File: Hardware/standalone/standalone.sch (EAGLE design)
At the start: 87 parts, among them Q2 32.768khz, U1 DMS3016SSS-13, U2 DMS3016SSS-13, U3 DMS3016SSS-13, U4 LM2575S-15, U5 NMOS_2N7002, U6 NMOS_2N7002, X1 KUSBVX, X2 KUSBVX

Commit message: Added item to hardware todo list
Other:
- note added: "TODO: - Change Caps to surface mount - Battery Bi-Directional Current Sense - Change Current Sense R - Swap 5V Diode to SMT - Power LED - Check if LCD R/W Pin is needed?"
- note removed: "TODO: - Change Caps to surface mount - Battery Bi-Directional Current Sense - Change Current Sense R - Swap 5V Diode to SMT - Power LED"
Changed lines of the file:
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@@
   - Change Current Sense R
   - Swap 5V Diode to SMT
-  - Power LED</text>
+  - Power LED
+  - Check if LCD R/W Pin is needed?</text>
 </plain>
 <instances>

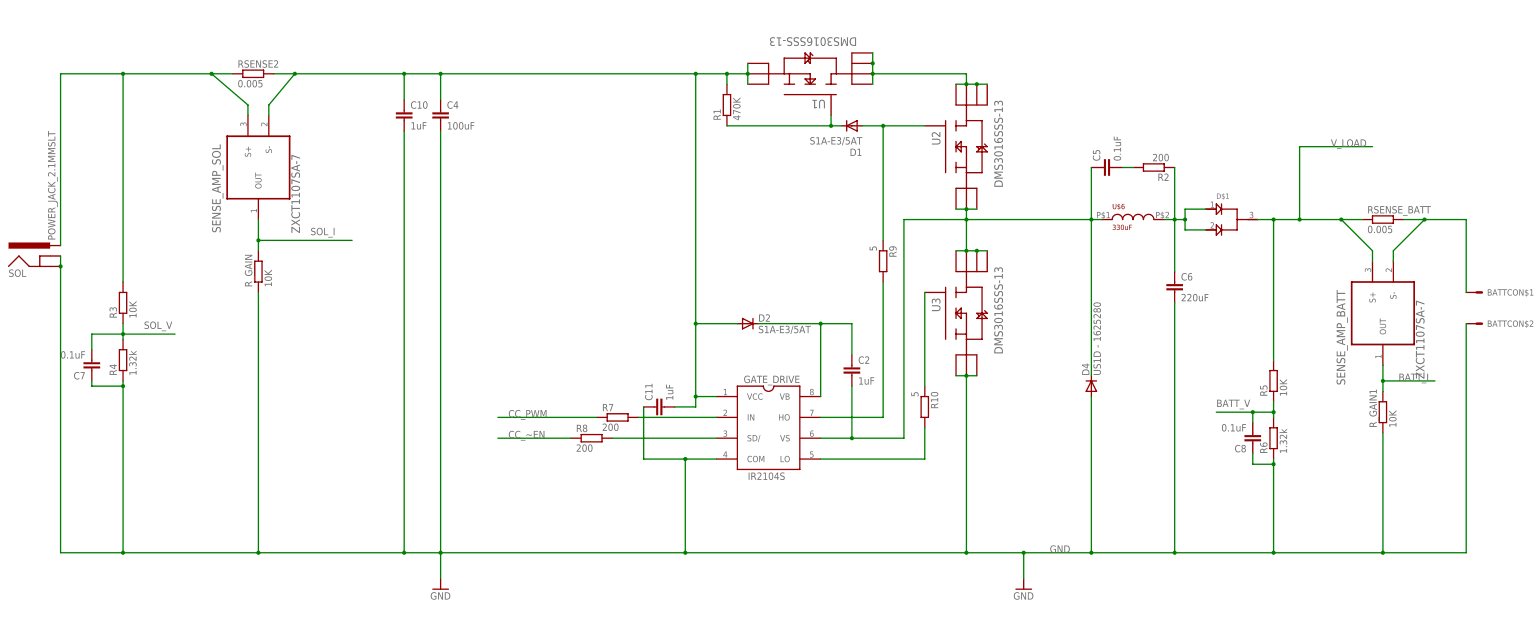
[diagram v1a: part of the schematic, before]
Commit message: Some Hardware Fixes
Fixed the Battery Connector.
Added more items to ToDo list
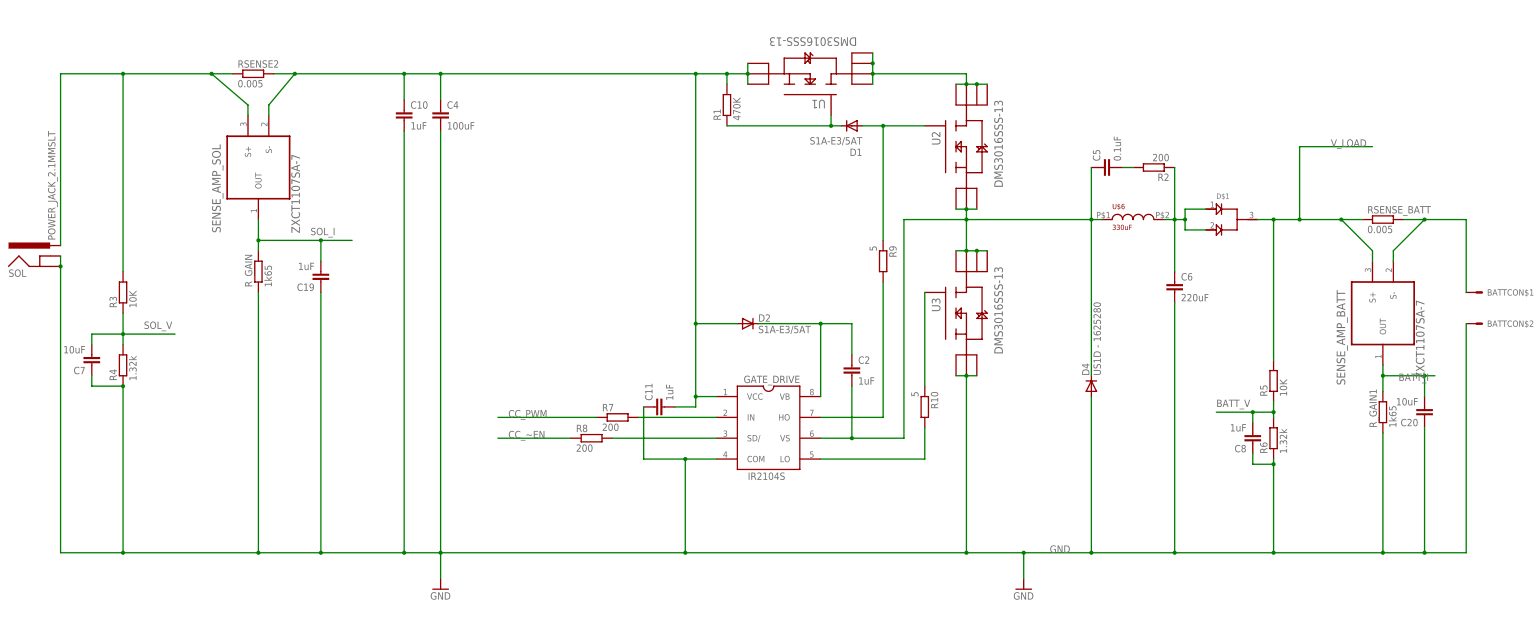
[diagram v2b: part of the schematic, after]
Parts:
- added C19: 1uF, resistor:C-EUC0805K
- added C20: 10uF, resistor:C-EUC0805K
- C7: value 0.1uF -> 10uF
- C8: value 0.1uF -> 1uF
- R_GAIN, R_GAIN1: value 10K -> 1k65
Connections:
- net BATT_I: now also C20.2
- net GND: now also C19.1, C20.1
- net SOL_I: now also C19.2
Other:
- note added: "TODO: - Change Caps to surface mount - Battery Bi-Directional Current Sense - Change Current Sense R - Swap 5V Diode to SMT - Power LED - Check if LCD R/W Pin is needed? - Add filtering (LC) to AVCC - Change Battery Diode to: 1336556 - Change Inductors and Cap for Buck - Remove U1 (Not needed) - Change Power Switch"
- note removed: "TODO: - Change Caps to surface mount - Battery Bi-Directional Current Sense - Change Current Sense R - Swap 5V Diode to SMT - Power LED - Check if LCD R/W Pin is needed?"
- moved on the sheet: C7, R3, R4
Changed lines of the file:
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@@
 <part name="R3" library="rcl" deviceset="R-EU_" device="M0805" value="10K"/>
 <part name="R4" library="rcl" deviceset="R-EU_" device="M0805" value="1.32k"/>
-<part name="C7" library="resistor" deviceset="C-EU" device="C0805K" value="0.1uF"/>
+<part name="C7" library="resistor" deviceset="C-EU" device="C0805K" value="10uF"/>
 <part name="R5" library="rcl" deviceset="R-EU_" device="M0805" value="10K"/>
 <part name="R6" library="rcl" deviceset="R-EU_" device="M0805" value="1.32k"/>
-<part name="C8" library="resistor" deviceset="C-EU" device="C0805K" value="0.1uF"/>
+<part name="C8" library="resistor" deviceset="C-EU" device="C0805K" value="1uF"/>
 <part name="R8" library="rcl" deviceset="R-EU_" device="M0805" value="200"/>
 <part name="R7" library="rcl" deviceset="R-EU_" device="M0805" value="200"/>
@@
 <part name="U$6" library="lib" deviceset="INDUC_BOURNES_SDR1806" device="" value="330uF"/>
 <part name="SENSE_AMP_SOL" library="equinox" deviceset="ZXCT1107SA-7" device=""/>
-<part name="R_GAIN" library="rcl" deviceset="R-EU_" device="M0805" value="10K"/>
+<part name="R_GAIN" library="rcl" deviceset="R-EU_" device="M0805" value="1k65"/>
 <part name="RSENSE_BATT" library="rcl" deviceset="R-EU_" device="R2512" value="0.005"/>
 <part name="SENSE_AMP_BATT" library="equinox" deviceset="ZXCT1107SA-7" device=""/>
-<part name="R_GAIN1" library="rcl" deviceset="R-EU_" device="M0805" value="10K"/>
+<part name="R_GAIN1" library="rcl" deviceset="R-EU_" device="M0805" value="1k65"/>
 <part name="GATE_DRIVE" library="equinox" deviceset="IR2104S" device=""/>
 <part name="U1" library="equinox" deviceset="DMS3016SSS-13" device=""/>
@@
 <part name="+3V9" library="supply1" deviceset="+3V3" device=""/>
 <part name="C3" library="resistor" deviceset="C-EU" device="C0805K" value="100nF"/>
+<part name="C19" library="resistor" deviceset="C-EU" device="C0805K" value="1uF"/>
+<part name="C20" library="resistor" deviceset="C-EU" device="C0805K" value="10uF"/>
 </parts>
 <sheets>
@@
   - Swap 5V Diode to SMT
   - Power LED
-  - Check if LCD R/W Pin is needed?</text>
+  - Check if LCD R/W Pin is needed?
+  - Add filtering (LC) to AVCC
+  - Change Battery Diode to: 1336556
+  - Change Inductors and Cap for Buck
+  - Remove U1 (Not needed)
+  - Change Power Switch</text>
 </plain>
 <instances>
@@
 <instance part="R2" gate="G$1" x="289.56" y="436.88" rot="R180"/>
 <instance part="C6" gate="G$1" x="294.64" y="408.94"/>
-<instance part="R3" gate="G$1" x="38.1" y="403.86" rot="R90"/>
-<instance part="R4" gate="G$1" x="38.1" y="389.89" rot="R90"/>
-<instance part="C7" gate="G$1" x="30.48" y="387.35" rot="R180"/>
+<instance part="R3" gate="G$1" x="38.1" y="406.4" rot="R90"/>
+<instance part="R4" gate="G$1" x="38.1" y="388.62" rot="R90"/>
+<instance part="C7" gate="G$1" x="30.48" y="388.62" rot="R180"/>
 <instance part="R5" gate="G$1" x="318.77" y="384.81" rot="R90"/>
 <instance part="R6" gate="G$1" x="318.77" y="370.84" rot="R90"/>
@@
 <instance part="+3V9" gate="G$1" x="101.6" y="121.92"/>
 <instance part="C3" gate="G$1" x="116.84" y="91.44" rot="R180"/>
+<instance part="C19" gate="G$1" x="86.36" y="408.94" rot="R180"/>
+<instance part="C20" gate="G$1" x="355.6" y="375.92" rot="R180"/>
 </instances>
 <busses>
@@
 <net name="SOL_V" class="0">
 <segment>
-<wire x1="38.1" y1="398.78" x2="38.1" y2="396.24" width="0.1524" layer="91"/>
-<wire x1="38.1" y1="396.24" x2="38.1" y2="394.97" width="0.1524" layer="91"/>
+<wire x1="38.1" y1="401.32" x2="38.1" y2="396.24" width="0.1524" layer="91"/>
+<wire x1="38.1" y1="396.24" x2="38.1" y2="393.7" width="0.1524" layer="91"/>
 <wire x1="38.1" y1="396.24" x2="30.48" y2="396.24" width="0.1524" layer="91"/>
-<wire x1="30.48" y1="396.24" x2="30.48" y2="392.43" width="0.1524" layer="91"/>
+<wire x1="30.48" y1="396.24" x2="30.48" y2="393.7" width="0.1524" layer="91"/>
 <wire x1="38.1" y1="396.24" x2="50.8" y2="396.24" width="0.1524" layer="91"/>
 <junction x="38.1" y="396.24"/>
@@
 <wire x1="71.12" y1="424.18" x2="71.12" y2="419.1" width="0.1524" layer="91"/>
 <wire x1="71.12" y1="419.1" x2="71.12" y2="416.56" width="0.1524" layer="91"/>
-<wire x1="71.12" y1="419.1" x2="93.98" y2="419.1" width="0.1524" layer="91"/>
+<wire x1="71.12" y1="419.1" x2="86.36" y2="419.1" width="0.1524" layer="91"/>
 <junction x="71.12" y="419.1"/>
+<pinref part="C19" gate="G$1" pin="2"/>
+<wire x1="86.36" y1="419.1" x2="93.98" y2="419.1" width="0.1524" layer="91"/>
+<wire x1="86.36" y1="414.02" x2="86.36" y2="419.1" width="0.1524" layer="91"/>
+<junction x="86.36" y="419.1"/>
 </segment>
 <segment>
@@
 <junction x="38.1" y="459.74"/>
 <wire x1="59.69" y1="459.74" x2="64.77" y2="459.74" width="0.1524" layer="91"/>
-<wire x1="38.1" y1="459.74" x2="38.1" y2="408.94" width="0.1524" layer="91"/>
+<wire x1="38.1" y1="459.74" x2="38.1" y2="411.48" width="0.1524" layer="91"/>
 <pinref part="R3" gate="G$1" pin="2"/>
 <pinref part="SENSE_AMP_SOL" gate="A" pin="S+"/>
@@
 <wire x1="22.86" y1="342.9" x2="38.1" y2="342.9" width="0.1524" layer="91"/>
 <wire x1="38.1" y1="342.9" x2="71.12" y2="342.9" width="0.1524" layer="91"/>
-<wire x1="71.12" y1="342.9" x2="106.68" y2="342.9" width="0.1524" layer="91"/>
+<wire x1="71.12" y1="342.9" x2="86.36" y2="342.9" width="0.1524" layer="91"/>
+<wire x1="86.36" y1="342.9" x2="106.68" y2="342.9" width="0.1524" layer="91"/>
 <wire x1="106.68" y1="342.9" x2="115.57" y2="342.9" width="0.1524" layer="91"/>
 <wire x1="106.68" y1="342.9" x2="106.68" y2="445.77" width="0.1524" layer="91"/>
@@
 <wire x1="175.26" y1="342.9" x2="243.84" y2="342.9" width="0.1524" layer="91"/>
 <wire x1="243.84" y1="342.9" x2="257.81" y2="342.9" width="0.1524" layer="91"/>
-<wire x1="38.1" y1="384.81" x2="38.1" y2="383.54" width="0.1524" layer="91"/>
-<wire x1="30.48" y1="384.81" x2="30.48" y2="383.54" width="0.1524" layer="91"/>
+<wire x1="30.48" y1="386.08" x2="30.48" y2="383.54" width="0.1524" layer="91"/>
 <wire x1="30.48" y1="383.54" x2="38.1" y2="383.54" width="0.1524" layer="91"/>
 <junction x="38.1" y="383.54"/>
@@
 <wire x1="318.77" y1="364.49" x2="318.77" y2="342.9" width="0.1524" layer="91"/>
 <pinref part="GATE_DRIVE" gate="G$1" pin="COM"/>
-<wire x1="365.76" y1="342.9" x2="345.44" y2="342.9" width="0.1524" layer="91"/>
+<wire x1="365.76" y1="342.9" x2="355.6" y2="342.9" width="0.1524" layer="91"/>
 <junction x="318.77" y="342.9"/>
+<wire x1="355.6" y1="342.9" x2="345.44" y2="342.9" width="0.1524" layer="91"/>
 <wire x1="345.44" y1="342.9" x2="318.77" y2="342.9" width="0.1524" layer="91"/>
 <pinref part="D4" gate="G$1" pin="A"/>
@@
 <junction x="71.12" y="342.9"/>
 <label x="264.16" y="342.9" size="1.778" layer="95"/>
+<pinref part="C19" gate="G$1" pin="1"/>
+<wire x1="86.36" y1="406.4" x2="86.36" y2="342.9" width="0.1524" layer="91"/>
+<junction x="86.36" y="342.9"/>
+<pinref part="C20" gate="G$1" pin="1"/>
+<wire x1="355.6" y1="373.38" x2="355.6" y2="342.9" width="0.1524" layer="91"/>
+<junction x="355.6" y="342.9"/>
 </segment>
 <segment>
@@
 <pinref part="SENSE_AMP_BATT" gate="A" pin="OUT"/>
 <pinref part="R_GAIN1" gate="G$1" pin="2"/>
-<wire x1="345.44" y1="388.62" x2="345.44" y2="384.81" width="0.1524" layer="91"/>
-<wire x1="345.44" y1="384.81" x2="345.44" y2="382.27" width="0.1524" layer="91"/>
-<wire x1="345.44" y1="384.81" x2="358.14" y2="384.81" width="0.1524" layer="91"/>
-<junction x="345.44" y="384.81"/>
-</segment>
-<segment>
+<wire x1="345.44" y1="388.62" x2="345.44" y2="386.08" width="0.1524" layer="91"/>
+<wire x1="345.44" y1="386.08" x2="345.44" y2="382.27" width="0.1524" layer="91"/>
+<wire x1="345.44" y1="386.08" x2="355.6" y2="386.08" width="0.1524" layer="91"/>
+<junction x="345.44" y="386.08"/>
+<pinref part="C20" gate="G$1" pin="2"/>
+<wire x1="355.6" y1="386.08" x2="358.14" y2="386.08" width="0.1524" layer="91"/>
+<wire x1="355.6" y1="381" x2="355.6" y2="386.08" width="0.1524" layer="91"/>
+<junction x="355.6" y="386.08"/>
+</segment>
+<segment>
